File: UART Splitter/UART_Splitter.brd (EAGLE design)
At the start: 17.4 x 20.3 mm, 6 parts, among them IC1 ATTINY10, U1 74HC4052

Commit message: UART Splitter
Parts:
- added C1, C2: 22pf, resistor:C0805K
- added C3, C4, C5: 1uF, resistor:C0805K
- added LED1, LED2, LED3, LED4, LED5, LED6, LED7, LED8: (no value), led:SML0603
- added Q1: 12mhz, crystal:HC49UP
- added R1, R2, R3: 10k, resistor:R0805W
- added R10, R11, R4, R5, R6, R7, R8, R9: (no value), resistor:R0805W
- moved IC1 57.7 mm to (65.9, 8.79), turned to 180 degrees
- moved U$2 44.9 mm to (40.6, 5.08), turned to 90 degrees
- moved U$1 43.6 mm to (52.1, 5.08), flipped to the top, turned to 180 degrees
- moved JP3 40.5 mm to (50.8, 22.9), turned to 0 degrees
- moved U1 39.9 mm to (48.3, 15.2), flipped to the bottom
- moved JP2 36.3 mm to (30.5, 22.9), turned to 0 degrees
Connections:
- net N$8 renamed TX
- net N$9 renamed RX
- new net N$10: C2.1, Q1.1, U$1.7
- new net N$11: C1.1, Q1.2, U$1.8
- new net N$12: IC1.4, R3.2
- new net N$14: LED8.A, R4.1
- new net N$15: LED7.A, R5.1
- new net N$16: LED6.A, R6.1
- new net N$17: LED5.A, R7.1
- new net N$18: LED4.A, R8.1
- new net N$19: LED3.A, R9.1
- new net N$20: LED2.A, R10.1
- new net N$21: LED1.A, R11.1
- new net N$5: R2.1, U1.10
- new net N$6: R1.1, U1.9
- new net N$7: U1.6
- new net N$8: IC1.1, R1.2
- new net N$9: IC1.3, R2.2
- new net RX0: JP3.1, LED1.C, U1.1
- new net RX1: JP3.5, U1.5
- new net RX2: JP2.1, U1.2
- new net RX3: JP2.5, U1.4
- new net TX0: JP3.2, U1.12
- new net TX1: JP3.6, U1.14
- new net TX2: JP2.2, U1.15
- new net TX3: JP2.6, U1.11
- new net VCC: JP2.4, JP2.8, JP3.4, JP3.8, R10.2, R11.2, R4.2, R5.2, R6.2, R7.2, R8.2, R9.2
- net GND: now also C1.2, C2.2, C3.2, C4.2, C5.2, JP2.3, JP2.7, JP3.3, JP3.7
- net N$2: now also C3.1, C4.1, C5.1
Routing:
- added copper zone on layer 1, net GND
- added copper zone on layer 16, net GND
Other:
- board size 17.4 x 20.3 mm -> 40.6 x 24.1 mm

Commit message: UART Splitter
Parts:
- added R12: 10k, resistor:R0402
- added S1: (no value), SparkFun-Electromechanical:TACTILE_SWITCH_SMD
- C1, C2, C3, C4, C5: device resistor:C0805K -> resistor:C0402K
- R1, R10, R11, R2, R3, R4, R5, R6, R7, R8, R9: device resistor:R0805W -> resistor:R0402
- moved LED5 91.2 mm to (35.5, 18.7)
- moved LED3 75.5 mm to (43.7, 18.7)
- moved LED4 75.4 mm to (47.5, 19.6)
- moved LED6 75.4 mm to (55.2, 19.6)
- moved LED7 75.4 mm to (59.0, 19.6)
- moved LED8 75.4 mm to (62.8, 19.6)
- moved R11 72.3 mm to (36.4, 16.0)
- moved R10 65.3 mm to (38.6, 16.0)
- moved LED2 62.5 mm to (52.9, 20.0)
- moved LED1 61.2 mm to (50.4, 19.9), turned to 270 degrees
- moved R9 52.0 mm to (47.3, 16.2), turned to 270 degrees
- moved R8 44.8 mm to (50.0, 16.2), turned to 270 degrees
- moved R7 37.3 mm to (53.0, 16.2), turned to 270 degrees
- moved R6 30.7 mm to (55.7, 16.2), turned to 270 degrees
- moved R5 24.6 mm to (58.7, 15.7), turned to 270 degrees
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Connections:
- new net N$13: R12.1, U1.6
- net GND: now also S1.3, S1.4
- net N$2: now also R1.2
- net N$6: no longer R1.1
- net N$7: now also IC1.3, R1.1, S1.1, S1.2; no longer U1.6
- net N$8: now also IC1.6, R12.2; no longer IC1.1, R1.2
- net N$9: now also IC1.1; no longer IC1.3

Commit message: UART Splitter
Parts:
- moved Q1 23.2 mm to (36.5, 9.30)
- moved LED6 22.2 mm to (33.0, 19.9), turned to 270 degrees
- moved R6 20.1 mm to (35.9, 19.5), turned to 0 degrees
- moved LED8 19.4 mm to (43.4, 20.5), turned to 180 degrees
- moved R7 19.3 mm to (33.8, 17.7), turned to 0 degrees
- moved R4 18.8 mm to (42.7, 18.2), turned to 270 degrees
- moved LED7 18.4 mm to (40.6, 20.4), turned to 180 degrees
- moved R5 17.6 mm to (41.2, 18.2)
- moved LED3 17.4 mm to (61.1, 20.3), turned to 270 degrees
- moved C2 16.0 mm to (33.3, 7.62), turned to 180 degrees
- moved LED4 15.9 mm to (63.4, 20.3), turned to 270 degrees
- moved IC1 15.6 mm to (57.9, 11.0), flipped to the bottom, turned to 90 degrees
- moved R11 15.1 mm to (51.4, 17.4), turned to 270 degrees
- moved R10 14.3 mm to (52.8, 17.4), turned to 270 degrees
- moved R9 14.3 mm to (61.6, 17.4)
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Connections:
- net N$14 renamed LED_TX3
- net N$15 renamed LED_RX3
- net N$16 renamed LED_TX2
- net N$17 renamed LED_RX2
- net N$18 renamed LED_TX1
- net N$19 renamed LED_RX1
- net N$20 renamed LED_TX0
- net N$21 renamed LED_RX0
- removed net N$1: U$1.1, U$2.GND
- removed net N$2: C3.1, C4.1, C5.1, IC1.5, R1.2, U$1.16, U$2.VBUS, U1.16
- net GND: now also U$1.1, U$2.GND
- net N$6: now also R3.1
- net RX1: now also LED3.C
- net RX2: now also LED5.C
- net RX3: now also LED7.C
- net TX0: now also LED2.C
- net TX1: now also LED4.C
- net TX2: now also LED6.C
- net TX3: now also LED8.C
- net VCC: now also C3.1, C4.1, C5.1, IC1.5, R1.2, U$1.16, U$2.VBUS, U1.16
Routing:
- net VCC: track 0.00 -> 84.3 mm, vias 0 -> 1
- net N$10: track 0.00 -> 22.1 mm
- net N$13: track 0.00 -> 21.8 mm
- net N$3: track 0.00 -> 16.1 mm
- net N$4: track 0.00 -> 15.6 mm
- net N$7: track 0.00 -> 13.7 mm, vias 0 -> 1
- net N$11: track 0.00 -> 13.2 mm
- net N$6: track 0.00 -> 10.3 mm
- net LED_RX2: track 0.00 -> 3.30 mm
- net N$9: track 0.00 -> 3.29 mm
- net RX3: track 0.00 -> 2.62 mm
- net N$12: track 0.00 -> 2.61 mm
- net TX3: track 0.00 -> 2.55 mm
- net N$8: track 0.00 -> 2.52 mm
- net N$5: track 0.00 -> 2.39 mm
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
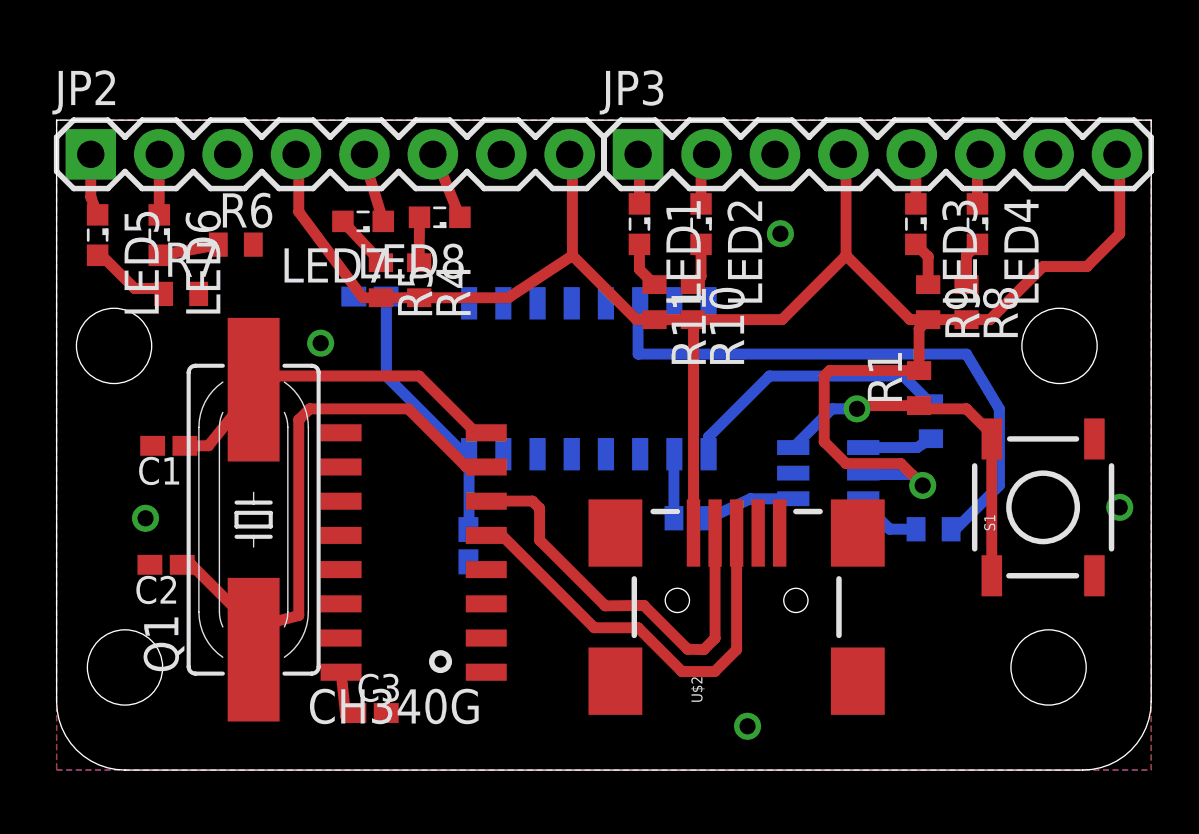
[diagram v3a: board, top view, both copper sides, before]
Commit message: Working on UART Splitter
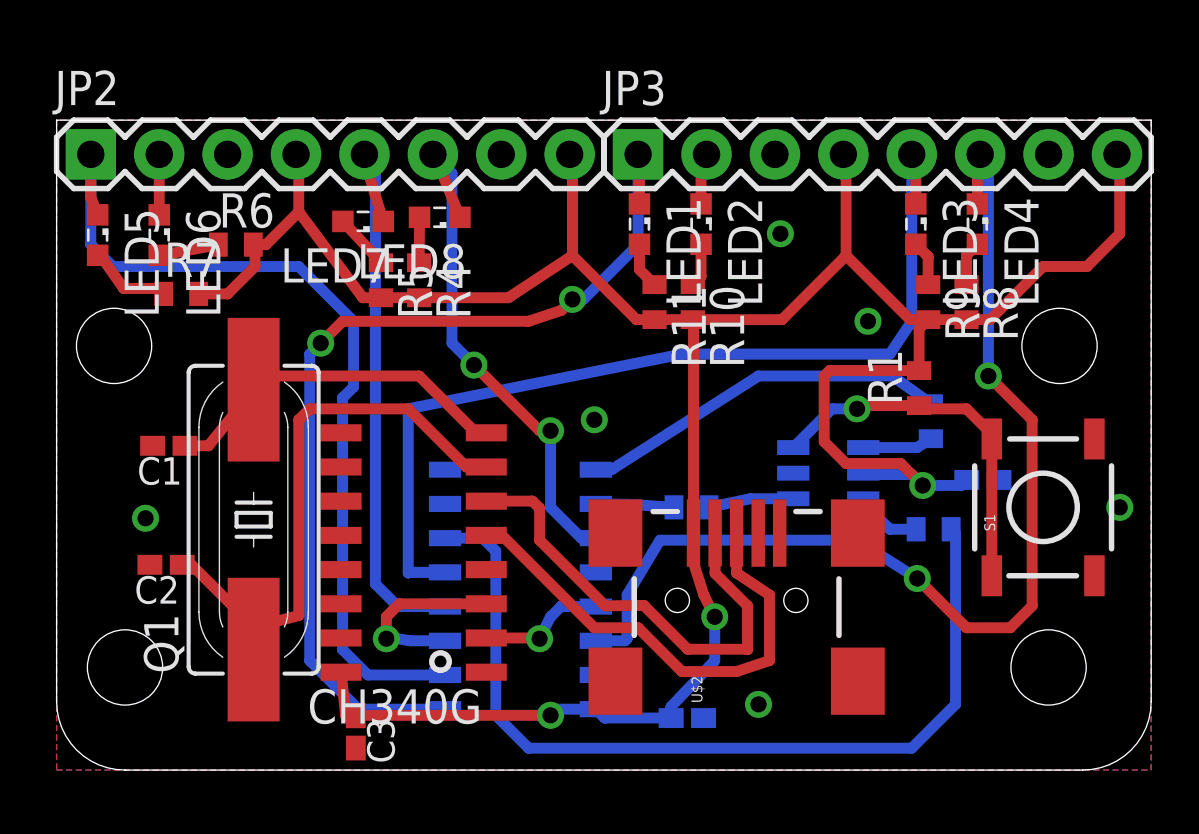
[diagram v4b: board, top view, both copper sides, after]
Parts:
- moved C5 19.6 mm to (52.6, 1.93), turned to 180 degrees
- moved C4 19.3 mm to (63.6, 10.8), turned to 180 degrees
- moved U1 8.23 mm to (46.4, 6.71), turned to 90 degrees
- moved C3 0.88 mm to (40.3, 1.42), turned to 270 degrees
- moved R2 0.41 mm to (52.8, 9.75)
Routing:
- net TX1: track 1.88 -> 40.2 mm, vias 0 -> 2
- net RX0: track 1.86 -> 36.1 mm, vias 0 -> 2
- net RX1: track 1.90 -> 35.1 mm
- net RX2: track 2.29 -> 33.1 mm
- net RX3: track 2.62 -> 21.7 mm
- net VCC: track 84.3 -> 102.0 mm, vias 1 -> 3
- net TX3: track 2.55 -> 19.9 mm, vias 0 -> 2
- net N$13: track 21.8 -> 33.0 mm
- net RX: track 0.00 -> 6.91 mm, vias 0 -> 1
- net TX: track 0.00 -> 4.81 mm, vias 0 -> 1
- net N$6: track 10.3 -> 13.8 mm
- net N$3: track 16.1 -> 18.1 mm
- net N$4: track 15.6 -> 17.5 mm
- net N$5: track 2.39 -> 2.90 mm

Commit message: UART
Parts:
- added U$3, U$4: (no value), SparkFun-Aesthetics:OSHW-LOGO-M
- LED1, LED3, LED5, LED7: value (none) -> GREEN
- LED2, LED4, LED6, LED8: value (none) -> BLUE
- R10, R11, R4, R5, R6, R7, R8, R9: value (none) -> 330
- moved C5 17.3 mm to (36.4, 7.82), turned to 0 degrees
- moved U1 4.90 mm to (43.3, 10.5), turned to 180 degrees
- moved C1 1.22 mm to (32.2, 12.0)
- moved C4 1.22 mm to (63.6, 9.55)
- moved IC1 1.22 mm to (57.9, 9.80)
- moved R10 1.22 mm to (52.8, 16.2)
- moved R11 1.22 mm to (51.4, 16.2)
- moved R2 1.22 mm to (52.8, 8.53)
- moved R3 1.22 mm to (61.7, 11.7)
- moved R4 1.22 mm to (42.7, 17.0)
- moved R5 1.22 mm to (41.2, 17.0)
- moved R8 1.22 mm to (63.0, 16.2)
- moved R9 1.22 mm to (61.6, 16.2)
- moved R12 1.22 mm to (61.8, 7.72)
- moved U$2 1.22 mm to (54.5, 5.08)
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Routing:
- net TX2: track 2.25 -> 27.9 mm, vias 0 -> 2
- net TX0: track 1.92 -> 25.3 mm, vias 0 -> 3
- net VCC: track 102.0 -> 124.3 mm, vias 3 -> 5
- net RX2: track 33.1 -> 19.8 mm, vias 0 -> 1
- net RX0: track 36.1 -> 25.1 mm, vias 2 -> 3
- net N$5: track 2.90 -> 13.1 mm
- net TX1: track 40.2 -> 49.3 mm, vias 2 -> 1
- net RX1: track 35.1 -> 26.7 mm, vias 0 -> 3
- net RX3: track 21.7 -> 14.4 mm, vias 0 -> 2
- net TX3: track 19.9 -> 24.0 mm, vias 2 -> 1
- net N$6: track 13.8 -> 17.9 mm
- net N$4: track 17.5 -> 15.0 mm, vias 0 -> 2
- net N$7: track 13.7 -> 16.2 mm
- net RX: track 6.91 -> 8.99 mm
- net N$10: track 22.1 -> 24.2 mm
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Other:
- board text added: "C. Thomas Brittain (C) ladvien.com UART Plex v01"
- board text added: "GND"
- board text added: "RX0"
- board text added: "RX1"
- board text added: "RX2"
- board text added: "RX3"
- board text added: "TX0"
- board text added: "TX1"
- board text added: "TX2"
- board text added: "TX3"
- board text added: "VCC"
